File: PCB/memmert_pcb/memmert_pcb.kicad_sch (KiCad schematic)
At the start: 3 parts, among them U1 PIC24FJXXXGL405_I_PT

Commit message: Progress on schematic
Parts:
- added C?: 10uF_6V3, Capacitor_SMD:C_0603_1608Metric, symbol USER_Cap_0603:10uF_6V3
- added C?: 100nF_50V, Capacitor_SMD:C_0603_1608Metric, symbol USER_Cap_0603:100nF_50V
- added J?: ICSP, USER_fp:ICSP, symbol USER_Connectors:ICSP
- added R?: 10k_5%, Resistor_SMD:R_0603_1608Metric, symbol USER_Res_0603:10k_5%
- C?: renamed from C1; value 100 nF -> 100nF_50V; symbol USER_Capacitors:100 nF -> USER_Cap_0603:100nF_50V; Part Number 0603_CAP_100NF -> 0603_CERCO_100NF50V
- C?: renamed from C2; value 100 nF -> 100nF_50V; symbol USER_Capacitors:100 nF -> USER_Cap_0603:100nF_50V; Part Number 0603_CAP_100NF -> 0603_CERCO_100NF50V
- U?: renamed from U1; Sourcing (none) -> https://www.digikey.de/de/products/detail/microchip-technol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
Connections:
- net +3V3: now also U?.15 (AVDD), C?.1, J?.2 (V_{DD}), R?.1
- net ICSPCLK: now reaches U?.11 (RB1)
- net ICSPCLK: now also J?.5 (ICSPCLK)
- net ICSPDAT: now reaches U?.12 (RB0)
- net ICSPDAT: now also J?.4 (ICSPDAT)
- net at U?.42 (VCAP): now also C?.1
- net ~{MCLR}: now reaches U?.6 (*MCLR)
- net ~{MCLR}: now also J?.1 (⁯‬V_{PP}/~{MCLR}), R?.2
- net GND renamed GNDD
- net GNDD: now also C?.2, C?.2, J?.3 (GND)

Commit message: Progress
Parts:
- added C?: 100nF_50V, Capacitor_SMD:C_0603_1608Metric, symbol USER_Cap_0603:100nF_50V
- added U?: MAX2202X, USER_fp:SOIC8_WIDE, symbol USER_Interface_IC:MAX2202X
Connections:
- net +3V3: now also C?.1, U?.3 (V_{DDA})
- net GNDD: now also C?.2, U?.4 (GNDA)
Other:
- note added: "ICSP Interface"
- moved on the sheet: C?, U?

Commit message: Progress
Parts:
- added C?: 100nF_50V, Capacitor_SMD:C_0603_1608Metric, symbol USER_Cap_0603:100nF_50V
- added T?: 750315226, USER_fp:Transformer_Wuerth_750315226, symbol USER_Transformer:750315226
- added U?: MAX253XSA, USER_fp:SOIC8, symbol USER_SMPS:MAX253XSA
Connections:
- net GNDD: now also C?.2, U?.2 (GND1), U?.7 (GND2)
- new net: T?.1, U?.1 (D1)
- new net: T?.2, U?.8 (D2)
- new net +5V: C?.1, T?.3
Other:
- moved on the sheet: C?, U?

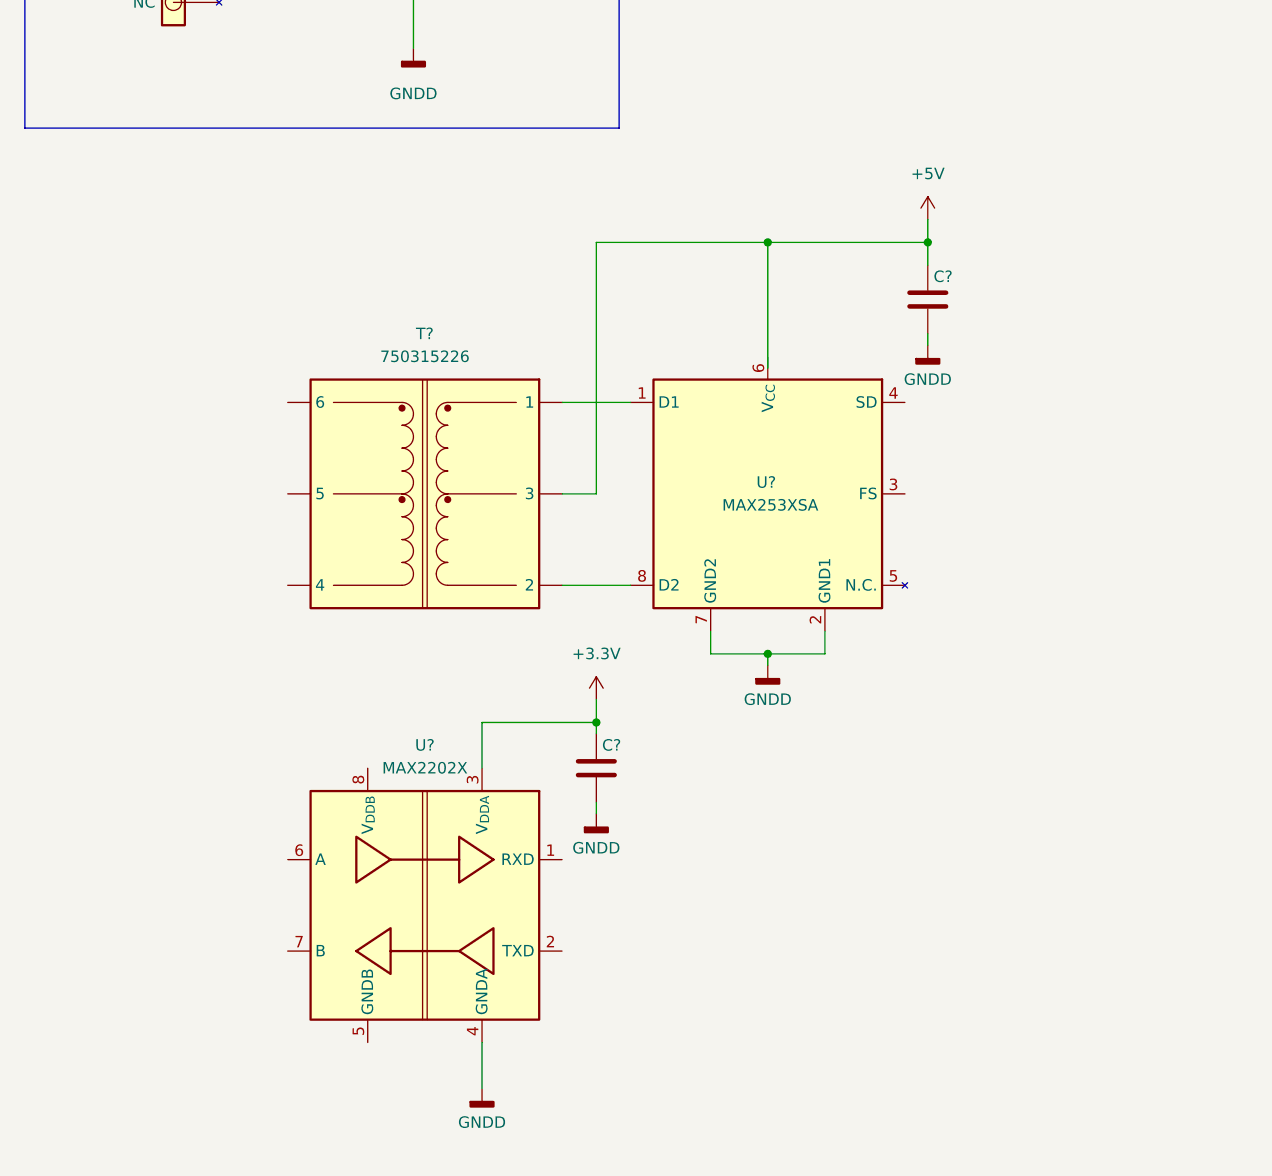
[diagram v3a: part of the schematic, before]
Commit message: LDO on the ISO side of the RS485 added
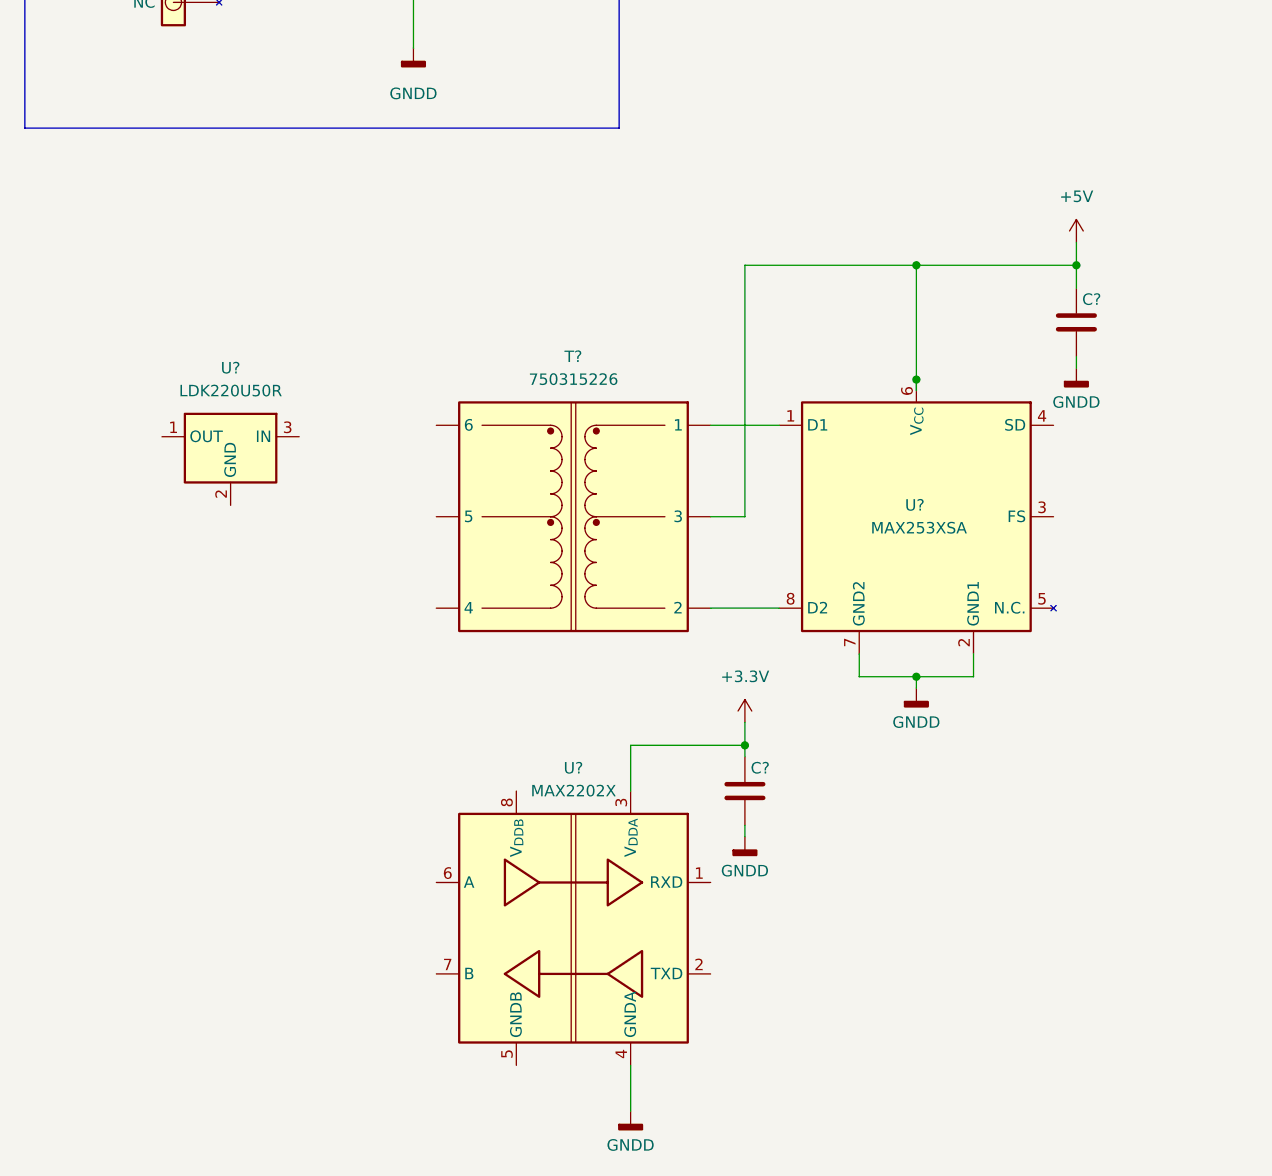
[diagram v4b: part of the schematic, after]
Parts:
- added U?: LDK220U50R, USER_fp:SOT-89, symbol USER_LDO:LDK220U50R
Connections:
- net +5V: now also U?.6 (V_{CC})
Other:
- moved on the sheet: C?, T?, U?
